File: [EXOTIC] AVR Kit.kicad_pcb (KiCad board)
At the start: 2 copper layers, 104.1 x 80 mm, 48 parts, among them J1 Barrel_Jack_Switch, J2 AVR-ISP-10, J3 USB_B, J4 Conn_01x08_Socket, J5 Conn_01x08_Socket, J6 Conn_01x09_Socket, J7 Conn_01x07_Socket, Q1 AO3401A, Q2 SI2302, SW1 SW_Push, SW2 SW_DPDT_x2, U1 ATmega32A-P, U2 AMS1117-5.0, U3 AMS1117-3.3, U4 LM324, U5 LM339, U6 CH340C, Y1 16 MHz

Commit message: Rev 3.2
Cleaned Up Schematic
Revised Layout
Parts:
- added R10: 0 Ω, Resistor_SMD:R_1206_3216Metric_Pad1.30x1.75mm_HandSolder, F.Cu at (174.0, 77.5)
- R7, R8: value 1 Ω -> 0.22 Ω
- moved R11 52.6 mm to (134.6, 101.6)
- moved R6 45.5 mm to (118.1, 86.4), turned to 90 degrees
- moved R4 39.1 mm to (118.1, 80.3), turned to 90 degrees
- moved J2 36.4 mm to (124.5, 99.1)
- moved R3 34.4 mm to (203.8, 58.4), turned to 0 degrees
- moved C4 34.2 mm to (168.9, 118.1)
- moved G*** 34.2 mm to (207.0, 124.5)
- moved SW1 34.2 mm to (134.1, 124.5)
- moved U2 34.2 mm to (168.9, 59.8)
- moved C11 34.2 mm to (133.3, 83.8)
- moved C6 34.2 mm to (168.9, 66.1)
- moved C7 34.2 mm to (179.1, 76.3)
- moved C8 34.2 mm to (163.8, 59.8)
- moved F1 34.2 mm to (157.5, 74.9)
- moved J3 34.2 mm to (128.3, 67.5)
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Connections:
- J2 pad 2: +5V -> +5V_NetTie
- L1 pad 2: +5V -> +5V_NetTie
- R11 pad 1: +3V3 -> +5V
- R11 pad 2: Net-(R11-Pad2) -> +5V_NetTie
- R9 pad 2: Net-(R11-Pad2) -> Net-(R10-Pad1)
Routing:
- net +5V: track 286.2 -> 211.4 mm
- net +5V_NetTie: track 0.00 -> 64.0 mm
- net Net-(R10-Pad1): track 0.00 -> 37.5 mm
- net Net-(R11-Pad2): track 35.0 -> 0.00 mm
- net Net-(SW2B-C): track 84.8 -> 75.9 mm
- net /MISO: track 154.9 -> 160.7 mm
- net Net-(U4D--): track 7.74 -> 13.3 mm
- net /SCK: track 169.7 -> 174.8 mm
- net /MOSI: track 75.7 -> 71.0 mm
- net -V_{In}: track 119.7 -> 122.6 mm
- net /~{RESET}: track 228.6 -> 225.9 mm
- net Net-(U5A--): track 46.5 -> 49.1 mm
- net Net-(U4A--): track 11.3 -> 12.8 mm
- net Net-(D1-K): track 4.78 -> 5.95 mm
- net VBUS: track 42.4 -> 43.4 mm
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
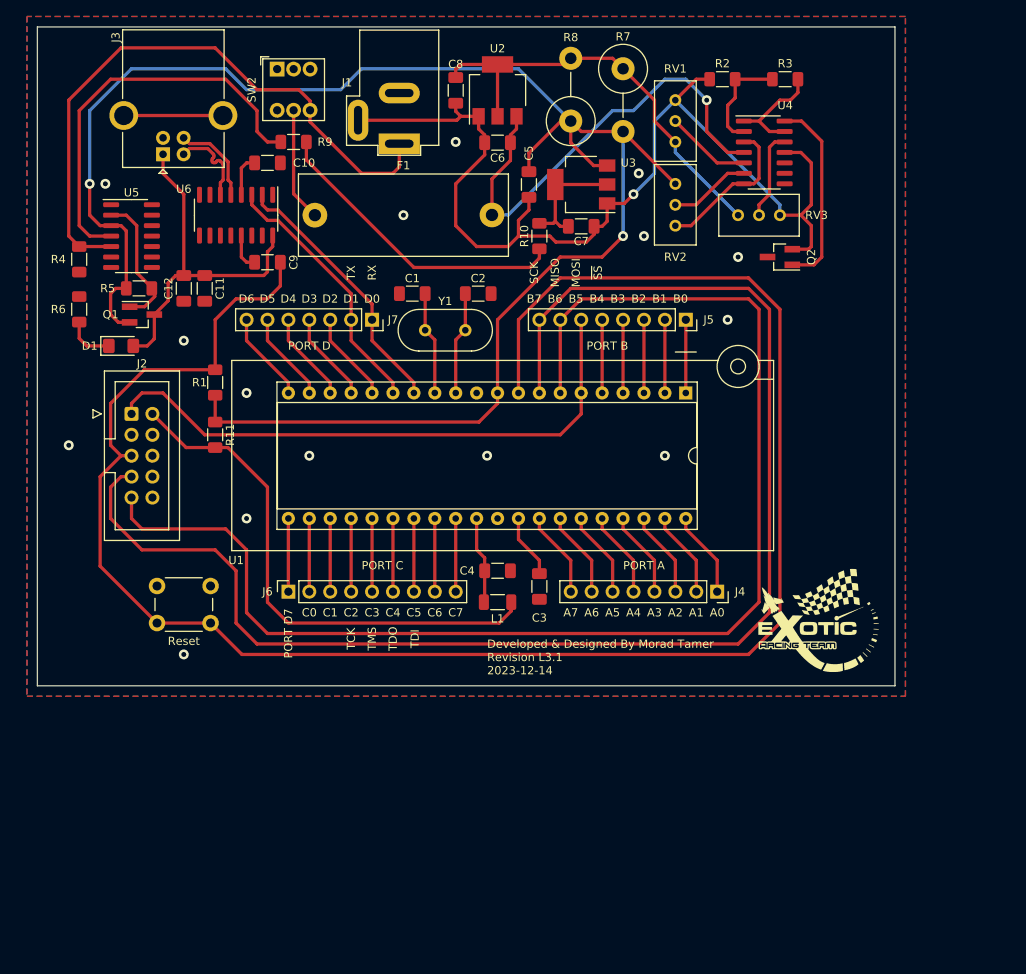
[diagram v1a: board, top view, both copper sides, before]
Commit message: Update [EXOTIC] AVR Kit.kicad_pcb
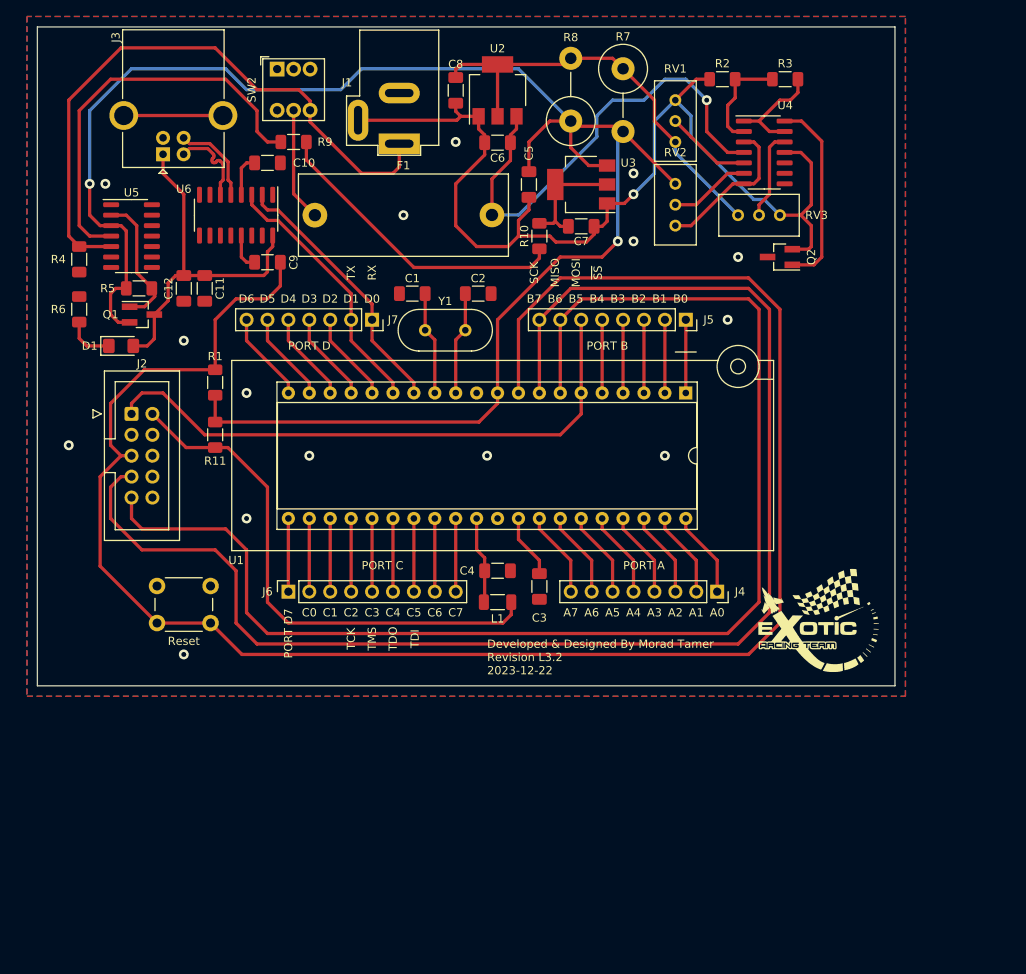
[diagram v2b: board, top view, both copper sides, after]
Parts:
- moved RV2 5.09 mm to (190.5, 71.1), turned to 90 degrees
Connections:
- net Net-(SW2B-C) renamed /Power Management Circuitry/V_{In} (Unfused)
- RV2 pad 1: Net-(U4A-+) -> +5V
- RV2 pad 3: +5V -> Net-(U4A-+)
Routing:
- net +V_{In}: track 56.5 -> 58.0 mm
- net +5V: track 211.4 -> 212.5 mm
- net -V_{In}: track 122.6 -> 123.3 mm

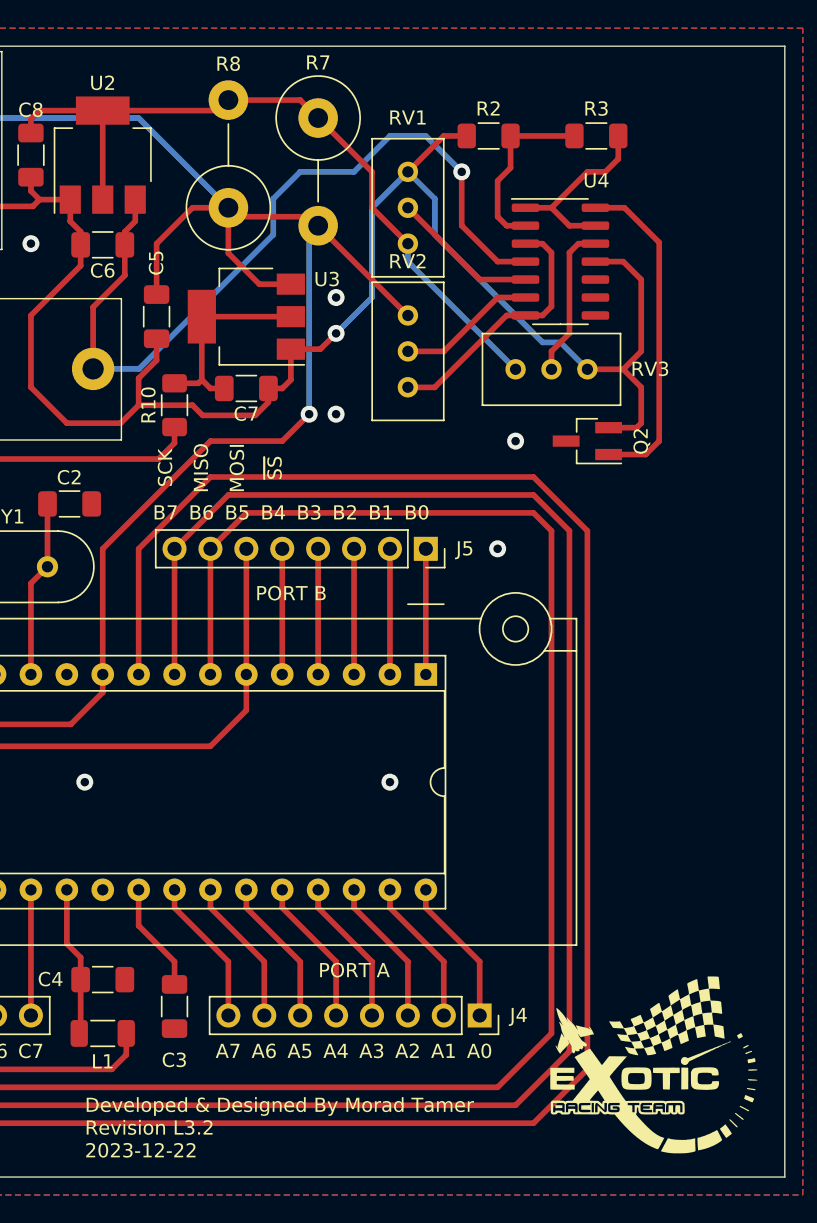
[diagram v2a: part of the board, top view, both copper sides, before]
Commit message: Added 5V and 3.3V O/P Pins
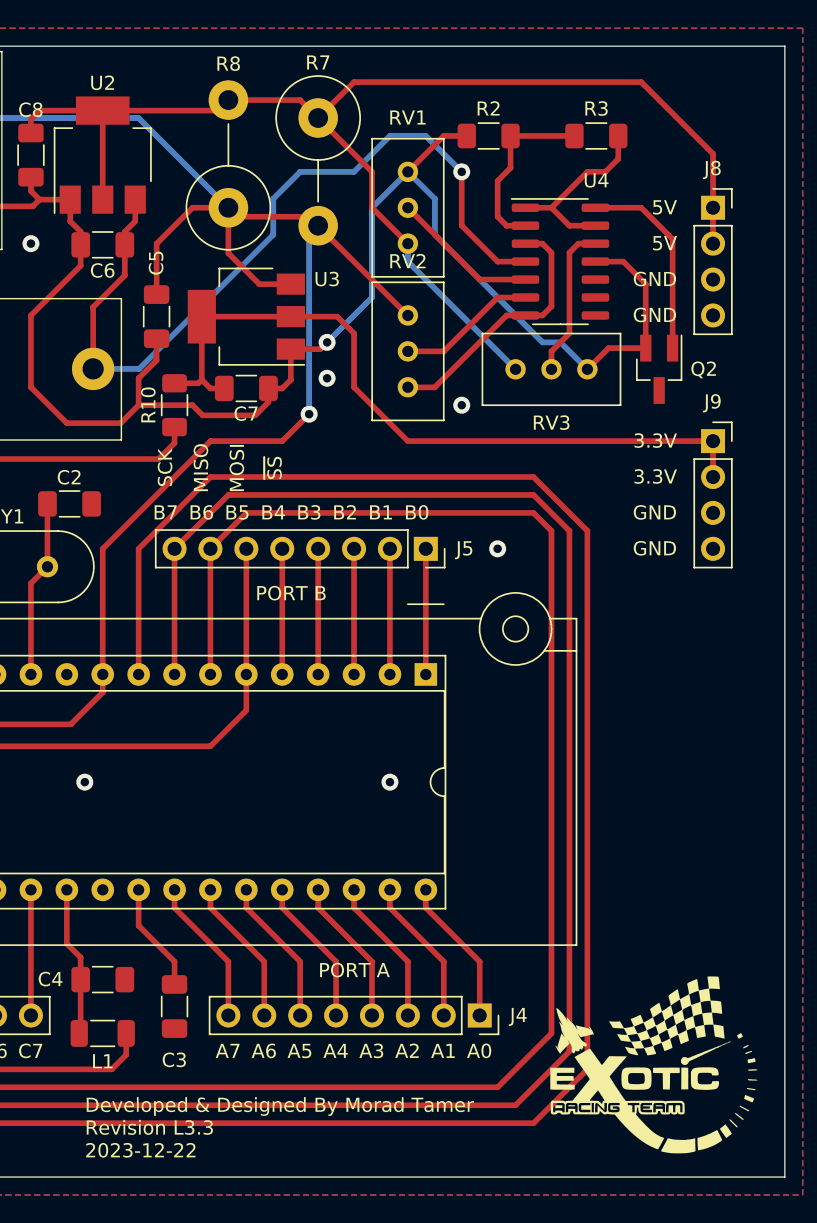
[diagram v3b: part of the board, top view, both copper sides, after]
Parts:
- added J8: Conn_01x04_Socket, Connector_PinSocket_2.54mm:PinSocket_1x04_P2.54mm_Vertical, F.Cu at (212.1, 63.5)
- added J9: Conn_01x04_Socket, Connector_PinSocket_2.54mm:PinSocket_1x04_P2.54mm_Vertical, F.Cu at (212.1, 80.0)
- moved Q2 7.18 mm to (208.3, 74.9), turned to -90 degrees
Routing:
- net +3V3: track 14.6 -> 52.9 mm
- net +5V_{OCP}: track 52.3 -> 89.7 mm
- net Net-(Q2-G): track 23.6 -> 14.1 mm
- net -V_{In}: track 123.3 -> 116.9 mm
- net GND: vias 15 -> 14
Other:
- board text added: "3.3V"
- board text added: "5V"
- board text added: "GND"

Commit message: Added My Initials
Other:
- board text added: "MT"
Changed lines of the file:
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@@
+    (effects (font (size 1 1) (thickness 0.15)))
+  )
+  (gr_text "MT" (at 157.48 72.39) (layer "B.Mask")
+    (effects (font (size 1 1) (thickness 0.15)) (justify mirror))
+  )
+  (gr_text "MT" (at 120.65 124.46) (layer "F.Mask")
     (effects (font (size 1 1) (thickness 0.15)))
   )

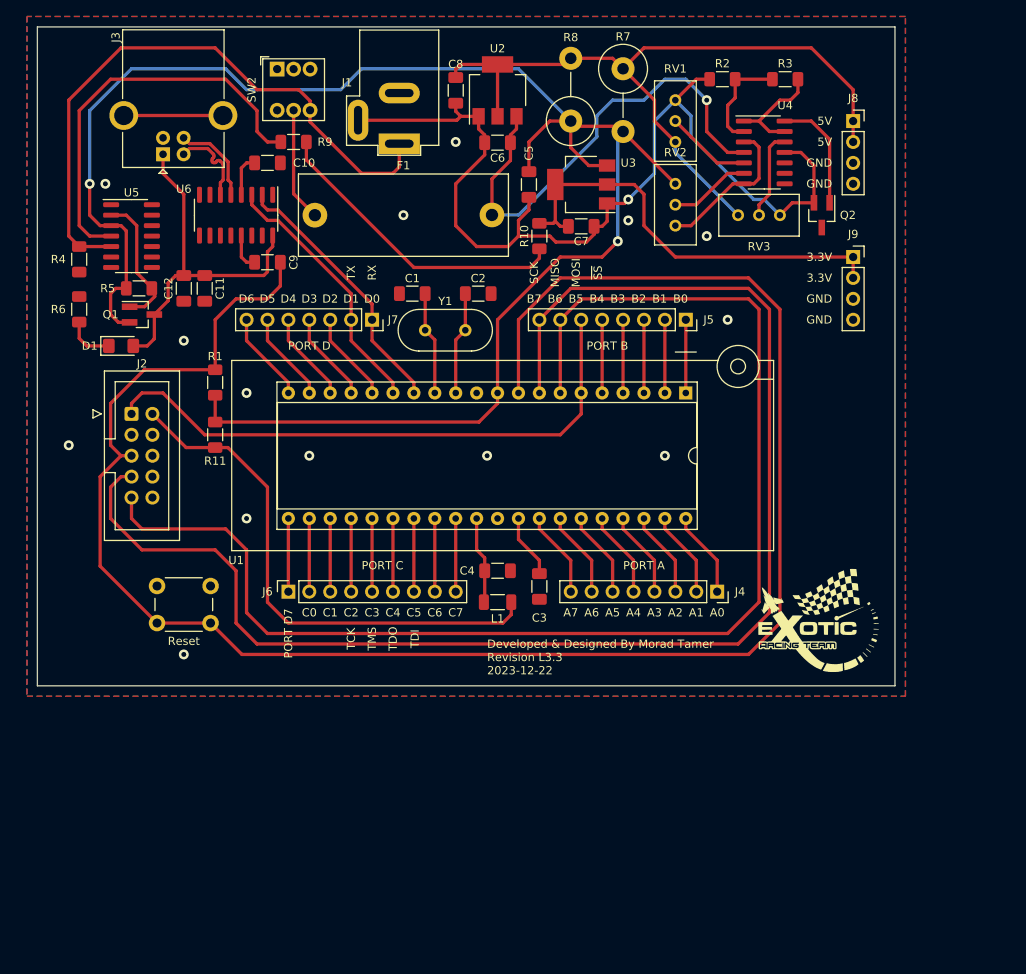
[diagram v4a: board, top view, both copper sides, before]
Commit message: Added I2C Labels
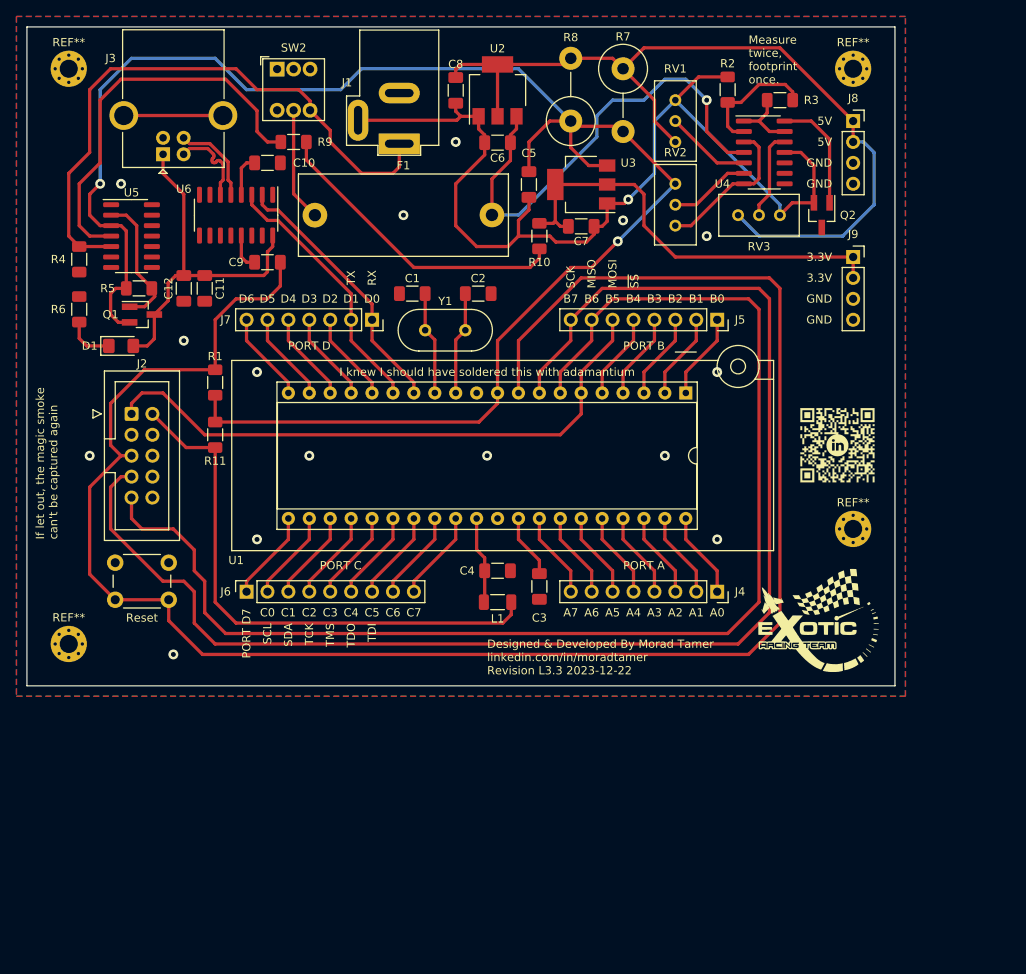
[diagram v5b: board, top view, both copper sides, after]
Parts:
- added G***: LOGO, LOGO, F.Cu at (210.2, 102.9)
- added REF**: MountingHole_2.2mm_M2_Pad_Via, MountingHole:MountingHole_2.2mm_M2_Pad_Via, F.Cu at (212.1, 113.0)
- added REF**: MountingHole_2.2mm_M2_Pad_Via, MountingHole:MountingHole_2.2mm_M2_Pad_Via, F.Cu at (212.1, 57.1)
- added REF**: MountingHole_2.2mm_M2_Pad_Via, MountingHole:MountingHole_2.2mm_M2_Pad_Via, F.Cu at (116.8, 127.0)
- added REF**: MountingHole_2.2mm_M2_Pad_Via, MountingHole:MountingHole_2.2mm_M2_Pad_Via, F.Cu at (116.8, 57.1)
- J4: value Conn_01x08_Socket -> Port A
- J5: value Conn_01x08_Socket -> Port B
- J6: value Conn_01x09_Socket -> Port C + D7
- J7: value Conn_01x07_Socket -> Port D
- J8: value Conn_01x04_Socket -> 5V Headers
- J9: value Conn_01x04_Socket -> 3.3 V Headers
- moved SW1 5.82 mm to (129.0, 121.6)
- moved J6 5.08 mm to (138.4, 120.7)
- moved J5 3.81 mm to (195.6, 87.6)
- moved R3 2.62 mm to (203.2, 61.0), turned to 180 degrees
- moved R2 1.42 mm to (196.8, 59.7), turned to -90 degrees
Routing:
- net +5V_{OCP}: track 89.7 -> 104.0 mm
- net Net-(U4D--): track 13.3 -> 8.43 mm
- net /~{RESET}: track 225.9 -> 229.8 mm
- net +5V: track 212.5 -> 209.1 mm
- net /MISO: track 160.7 -> 157.8 mm
- net /Power Management Circuitry/V_{In} (Unfused): track 75.9 -> 73.0 mm
- net +5V_NetTie: track 64.2 -> 67.0 mm
- net Net-(U4A--): track 12.8 -> 15.3 mm
- net /SCK: track 174.8 -> 172.6 mm
- net /TDO: track 8.89 -> 11.0 mm
- net /TDI: track 8.89 -> 11.0 mm
- net /PC7: track 8.89 -> 11.0 mm
- net /PC1: track 8.89 -> 11.0 mm
- net /PC0: track 8.89 -> 11.0 mm
- net /TMS: track 8.89 -> 11.0 mm
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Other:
- board size 104.1 x 80 mm -> 105.4 x 80 mm
- board text added: "Center Positive"
- board text added: "Designed & Developed By Morad Tamer linkedin.com/in/moradtamer Revision ${REVISION} ${ISSUE_DATE}"
- board text added: "I knew I should have soldered this with adamantium"
- board text added: "If let out, the magic smoke can't be captured again"
- board text added: "Measure twice, footprint once."
- board text added: "SCL"
- board text added: "SDA"
- board text removed: "Developed & Designed By Morad Tamer Revision ${REVISION} ${ISSUE_DATE}"
